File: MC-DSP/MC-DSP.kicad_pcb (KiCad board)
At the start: 6 copper layers, 160 x 100 mm, 168 parts, among them J1 374385, J80 5-1634513-1, J81 5-1634513-1, J82 5-1634513-1, SW1 SW_SPDT, T1 ERRORSTS, U1 TMS320F28388DZWT, U10 ECS-2520MV-xxx-xx, U12 BU4831F-TR, U13 BU4811G-TR, U2 SBH41-NBPB-D10-ST-BK, U20 R-78E3.3-1.0, U200 FT2232HL, U201 TPD2S017, U202 USB_B, U203 AZ1117-3.3, U204 ISO7730DW, U205 ISO7730DW, U206 ISO7730DW, U207 Crystal_GND24, U21 R-78B1.2-2.0, U60 OPA365xxD, U61 OPA365xxD, U62 OPA365xxD, U63 OPA365xxD, U64 OPA365xxD, U65 MAX6126AASA, U80 OPA365xxD, U81 OPA365xxD, U82 OPA365xxD

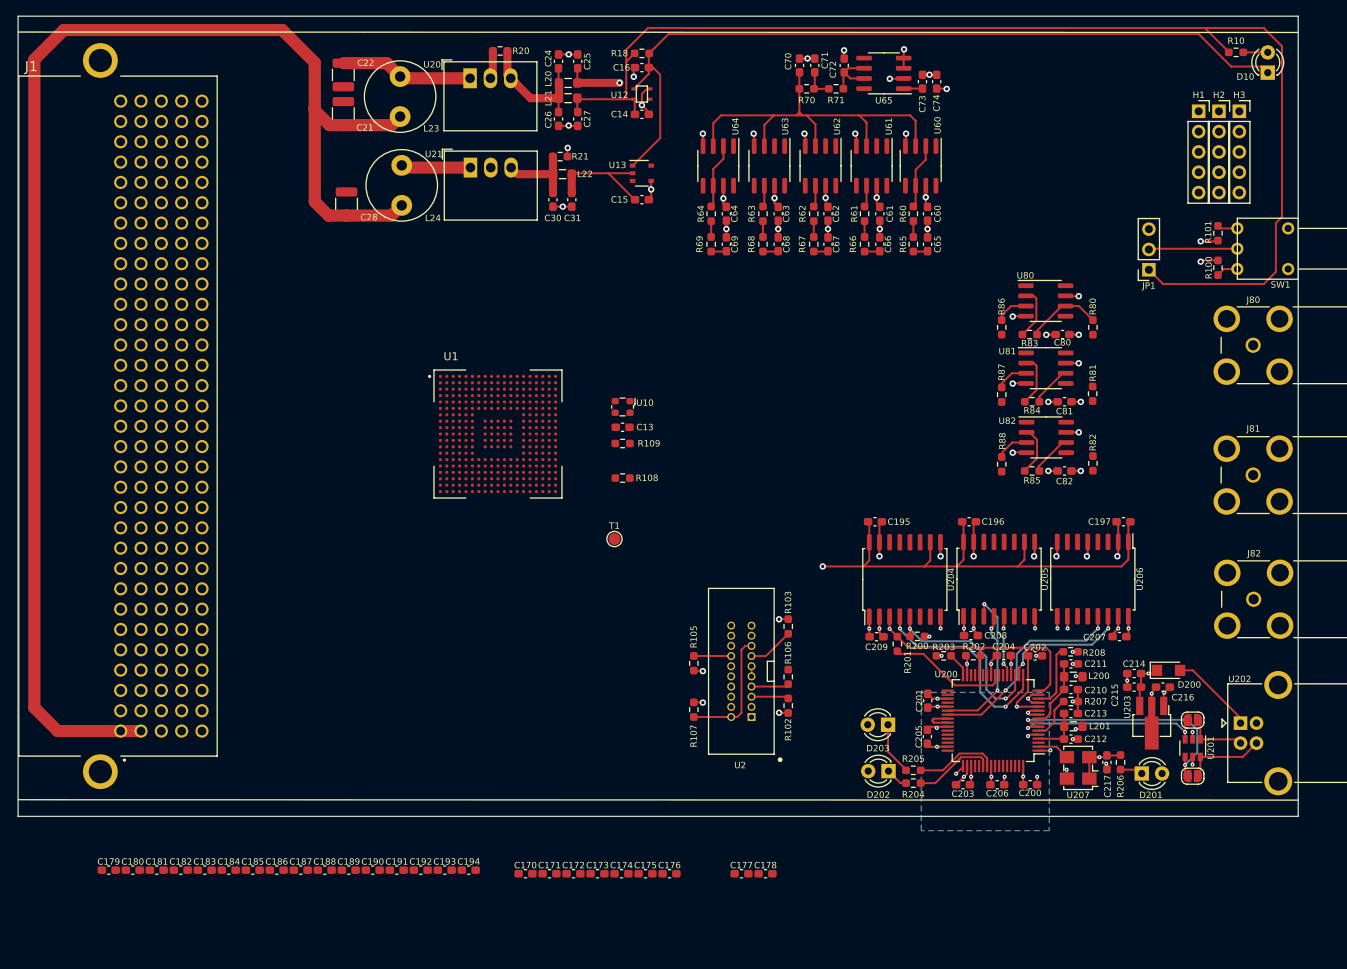
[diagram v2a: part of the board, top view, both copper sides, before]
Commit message: Total overhaul of power planes. Routed whole Analog section, middle of digital section.
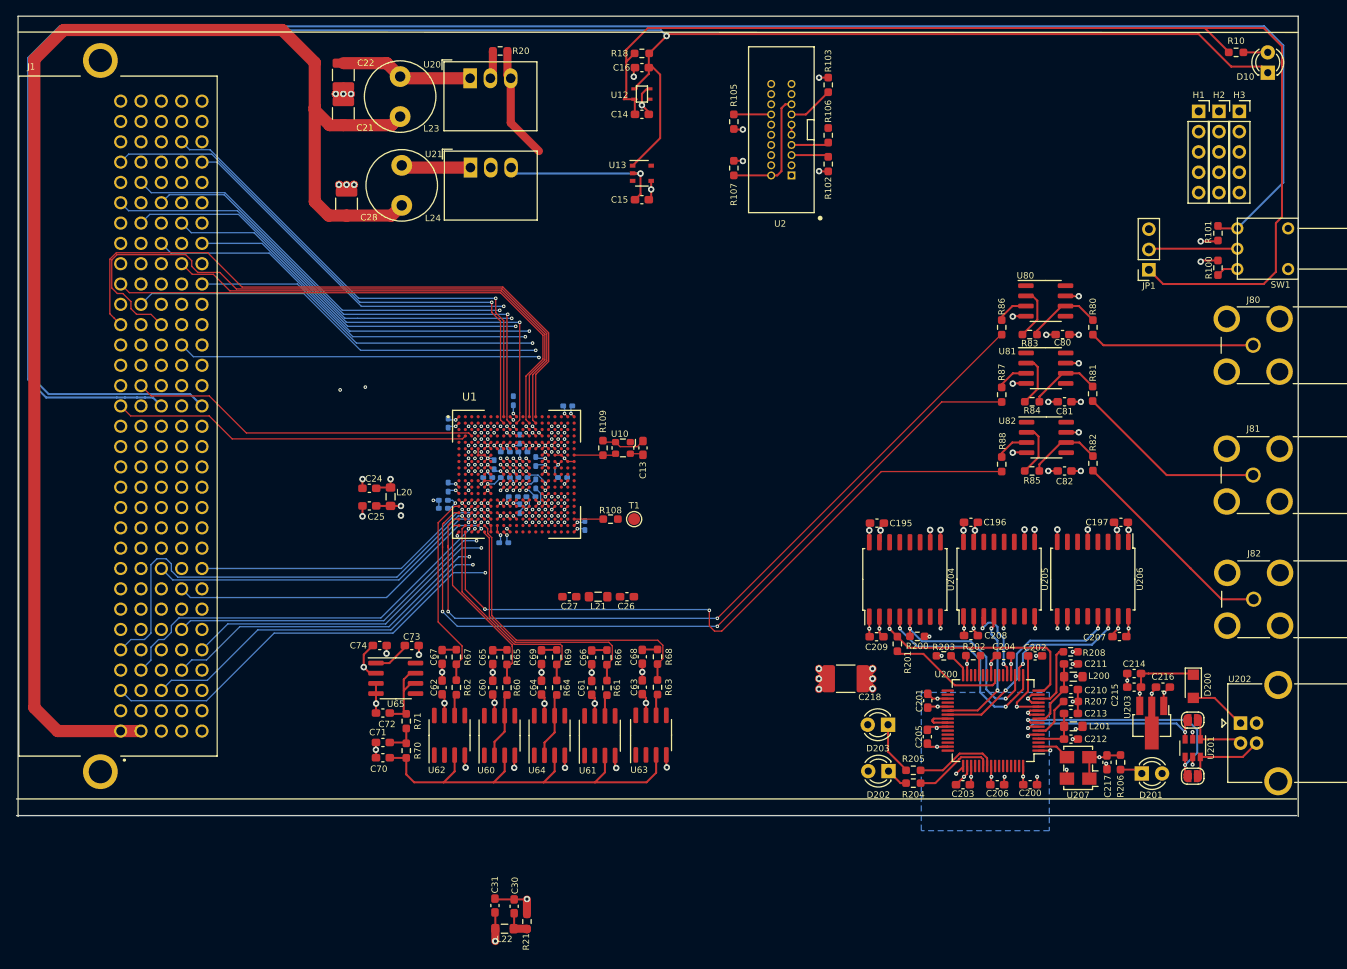
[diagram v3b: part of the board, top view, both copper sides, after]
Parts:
- removed C176, C192, C193, C194: 0.1uF, Capacitor_SMD:C_0603_1608Metric_Pad1.08x0.95mm_HandSolder
- added C218: 10pF 3000V, Capacitor_SMD:C_1812_4532Metric_Pad1.57x3.40mm_HandSolder, F.Cu at (204.6, 94.5)
- C170, C171, C172, C173, C174, C175, C177, C178, C179, C180, C181, C182, C183, C184, C185, C186, C187, C188, C189, C190, C191: footprint Capacitor_SMD:C_0603_1608Metric_Pad1.08x0.95mm_HandSolder -> Capacitor_SMD:C_0402_1005Metric_Pad0.74x0.62mm_HandSolder; moved to B.Cu
- moved C70 101.0 mm to (146.7, 104.4), turned to 0 degrees
- moved C71 100.4 mm to (146.7, 102.5), turned to 0 degrees
- moved C72 99.4 mm to (146.7, 98.8), turned to 0 degrees
- moved C74 99.1 mm to (146.3, 90.4), turned to 180 degrees
- moved U65 97.2 mm to (148.3, 94.5), turned to 0 degrees
- moved R70 96.7 mm to (149.6, 103.5), turned to 270 degrees
- moved R21 95.7 mm to (164.7, 124.9), turned to 90 degrees
- moved R71 95.6 mm to (149.6, 99.9), turned to 270 degrees
- moved C73 95.1 mm to (150.3, 90.4), turned to 180 degrees
- moved L22 94.6 mm to (161.9, 125.8), turned to 0 degrees
- moved C31 88.7 mm to (160.7, 122.9), turned to 90 degrees
- moved U60 88.5 mm to (161.3, 101.7), turned to 90 degrees
- moved C30 88.5 mm to (163.1, 123.0), turned to 270 degrees
- moved U62 84.9 mm to (155.0, 101.6), turned to 90 degrees
- moved C60 80.4 mm to (160.4, 95.7), turned to 270 degrees
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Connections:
- C15 pad 1: +1V2 -> /Voltage Regulators/SYS_1.2V
- C179 pad 2: +3V3 -> VDD
- C180 pad 2: +3V3 -> VDD
- C181 pad 2: +3V3 -> VDD
- C182 pad 2: +3V3 -> VDD
- C183 pad 2: +3V3 -> VDD
- C184 pad 2: +3V3 -> VDD
- C185 pad 2: +3V3 -> VDD
- C186 pad 2: +3V3 -> VDD
- C187 pad 2: +3V3 -> VDD
- C188 pad 2: +3V3 -> VDD
- C189 pad 2: +3V3 -> VDD
- C190 pad 2: +3V3 -> VDD
- C191 pad 2: +3V3 -> VDD
- C21 pad 1: VDD -> +24V
- C24 pad 2: Net-(C24-Pad2) -> +3V3
- C26 pad 2: Net-(C24-Pad2) -> +3V3
- C27 pad 1: +3V3 -> VDD
- C28 pad 1: VDD -> +24V
- C30 pad 2: Net-(C30-Pad2) -> /Voltage Regulators/SYS_1.2V
- C80 pad 2: VDDA -> Net-(C80-Pad2)
- C81 pad 2: VDDA -> Net-(C80-Pad2)
- C82 pad 2: VDDA -> Net-(C80-Pad2)
- J1 pad A1: VDD -> +24V
- J1 pad B1: VDD -> +24V
- L20 pad 2: Net-(C24-Pad2) -> +3V3
- L21 pad 1: +3V3 -> VDD
- L21 pad 2: Net-(C24-Pad2) -> +3V3
- L22 pad 2: Net-(C30-Pad2) -> /Voltage Regulators/SYS_1.2V
- L23 pad 1: VDD -> +24V
- L24 pad 1: VDD -> +24V
- R20 pad 1: Net-(C24-Pad2) -> +3V3
- R21 pad 1: Net-(C30-Pad2) -> /Voltage Regulators/SYS_1.2V
- U1 pad A18: +3V3 -> VDD
- U1 pad A9: +3V3 -> VDD
- U1 pad B1: +3V3 -> VDD
- U1 pad E10: +3V3 -> VDD
- U1 pad E13: +3V3 -> VDD
- U1 pad E16: +3V3 -> VDD
- U1 pad E7: +3V3 -> VDD
- U1 pad F10: +3V3 -> VDD
- U1 pad F13: +3V3 -> VDD
- U1 pad F16: +3V3 -> VDD
- U1 pad F4: +3V3 -> VDD
- U1 pad F7: +3V3 -> VDD
- U1 pad G4: +3V3 -> VDD
- U1 pad G5: +3V3 -> VDD
- U1 pad G6: +3V3 -> VDD
- U1 pad H16: +3V3 -> VDD
- U1 pad H17: +3V3 -> VDD
- U1 pad H5: +3V3 -> VDD
- U1 pad H6: +3V3 -> VDD
- U1 pad L14: +3V3 -> VDD
- U1 pad L15: +3V3 -> VDD
- U1 pad M1: +3V3 -> VDD
- U1 pad M5: +3V3 -> VDD
- U1 pad M6: +3V3 -> VDD
- U1 pad N14: +3V3 -> VDD
- U1 pad N15: +3V3 -> VDD
- U1 pad P6: +3V3 -> VDDA
- U1 pad P9: +3V3 -> VDD
- U1 pad R11: +3V3 -> VDD
- U1 pad R12: +3V3 -> VDD
- U1 pad R6: +3V3 -> VDDA
- U1 pad R9: +3V3 -> VDD
- U1 pad V19: +3V3 -> VDD
- U1 pad W8: +3V3 -> VDD
- U13 pad 2: +1V2 -> /Voltage Regulators/SYS_1.2V
- U20 pad 3: Net-(C24-Pad2) -> +3V3
- U21 pad 3: Net-(C30-Pad2) -> /Voltage Regulators/SYS_1.2V
- U80 pad 7: VDDA -> +3V3
- U81 pad 7: VDDA -> +3V3
- U82 pad 7: VDDA -> +3V3
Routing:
- net /Emitter_Enable: track 2.55 -> 245.6 mm
- net +24V: track 0.00 -> 175.6 mm
- net /Safe_State: track 100.0 -> 243.4 mm, vias 0 -> 1
- net VDD: track 175.6 -> 35.1 mm, vias 0 -> 17
- net /DAC to BNC/DAC_A: track 0.00 -> 97.2 mm, vias 0 -> 2
- net /DAC to BNC/DAC_B: track 0.00 -> 96.1 mm, vias 0 -> 2
- net /DAC to BNC/DAC_C: track 0.00 -> 85.8 mm, vias 0 -> 2
- net /EPWM3B: track 0.00 -> 83.3 mm
- net GND: track 79.5 -> 160.6 mm, vias 37 -> 100
- net /EPWM3A: track 0.00 -> 79.2 mm
- net /EPWM10B: track 0.00 -> 70.2 mm, vias 0 -> 1
- net /EPWM8A: track 0.00 -> 70.0 mm, vias 0 -> 2
- net /SD2_D1: track 0.00 -> 69.4 mm, vias 0 -> 1
- net /EPWM9B: track 0.00 -> 67.7 mm, vias 0 -> 2
- net /EPWM5B: track 0.00 -> 67.5 mm
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- added copper zone on In3.Cu, net +1V2
- added copper zone on In2.Cu, net VDD
- removed copper zone on In4.Cu, net EMU_GND
- removed copper zone on In4.Cu, net GND
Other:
- board size 160 x 100 mm -> 160.2 x 100 mm
- net class Default: clearance 0.2 -> 0.10922; via_dia 0.8 -> 0.508; via_drill 0.4 -> 0.2032
- rule trace_clearance: 0.2 -> 0.10922
- rule trace_min: 0.1524 -> 0.1016
- rule via_min_drill: 0.3 -> 0.2
- rule via_min_size: 0.2032 -> 0.4
- board text removed: "Mark Qs: how many layers? how to do layer stackup? how to fit vias under the dsp? what to do about DSP Caps?"
